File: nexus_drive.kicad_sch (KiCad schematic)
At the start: 0 parts

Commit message: Add phase power section to schematic from moteus x1
Three half-bridge sheets (FDMT80080DC pair, 0.5 mOhm shunt, Kelvin net
ties, gate clamp, phase pad) and the 36x 4.7uF DC-link bank, copied from
mjbots moteus hw/x1 (Apache-2.0) with attribution in NOTICE.md.

Co-Authored-By: Claude Opus 5.5 <noreply@anthropic.com>
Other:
- added sheet Bulk Capacitance (bulk_capacitance.kicad_sch)
- added sheet H Bridge A (h_bridge.kicad_sch)
- added sheet H Bridge B (h_bridge.kicad_sch)
- added sheet H Bridge C (h_bridge.kicad_sch)
- note added: "0.1 uF 100 V local decoupling, BAT41 low-side gate clamp, Kelvin net ties to SPx/SNx, M2.5 phase output pad."
- note added: "Bulk Capacitance = 36x 4.7 uF 100 V X7R DC-link bank between V+ and GNDPWR (global nets)."
- note added: "Copied from mjbots moteus-x1 r1 (Apache-2.0): https://github.com/mjbots/moteus/tree/main/hw/x1"
- note added: "Each H Bridge sheet = one half-bridge: 2x FDMT80080DC (80 V), 0.5 mOhm low-side shunt,"
- note added: "GHx/SHx/GLx/SPx/SNx connect to the DRV8353S gate driver sheet (to be added)."
- note added: "PHASE POWER STAGE"
- note added: "Still to add (see docs/power-stage.md): input TVS, bulk electrolytic, anti-spark connector, voltage dividers."
- title: (none) -> Nexus Drive

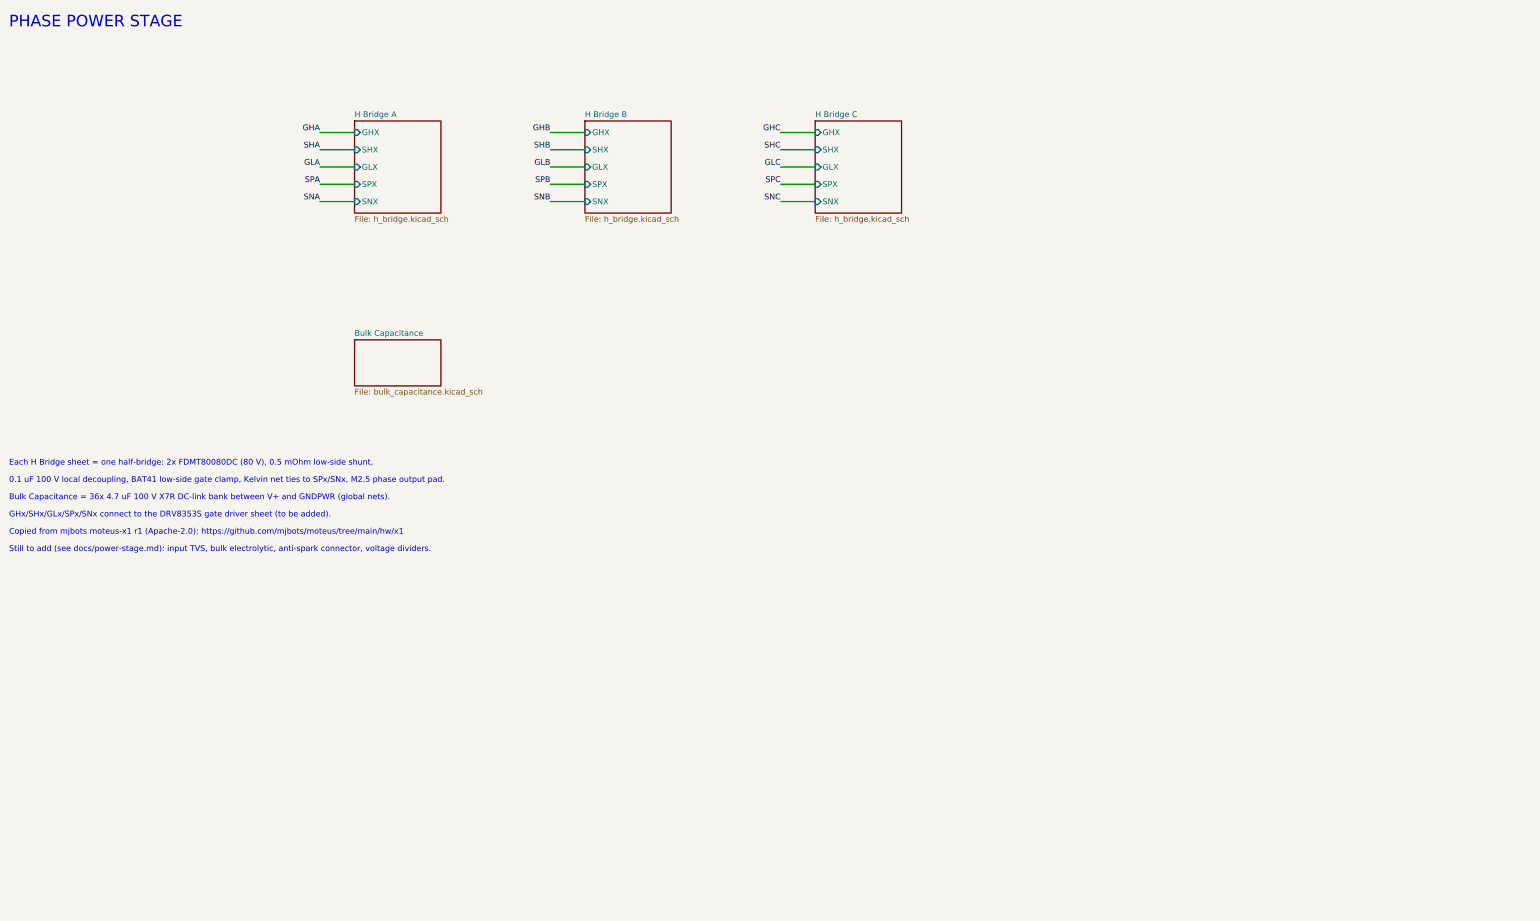
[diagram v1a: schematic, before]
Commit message: Add DRV8353S gate driver and current-sense filter sheets from moteus x1
Gate driver and current-sense RC sheets copied from mjbots moteus hw/x1
(Apache-2.0). Root sheet moved to A3 and rewired; netlist matches moteus
pin-for-pin for the driver and power stage.

Co-Authored-By: Claude Opus 5.5 <noreply@anthropic.com>
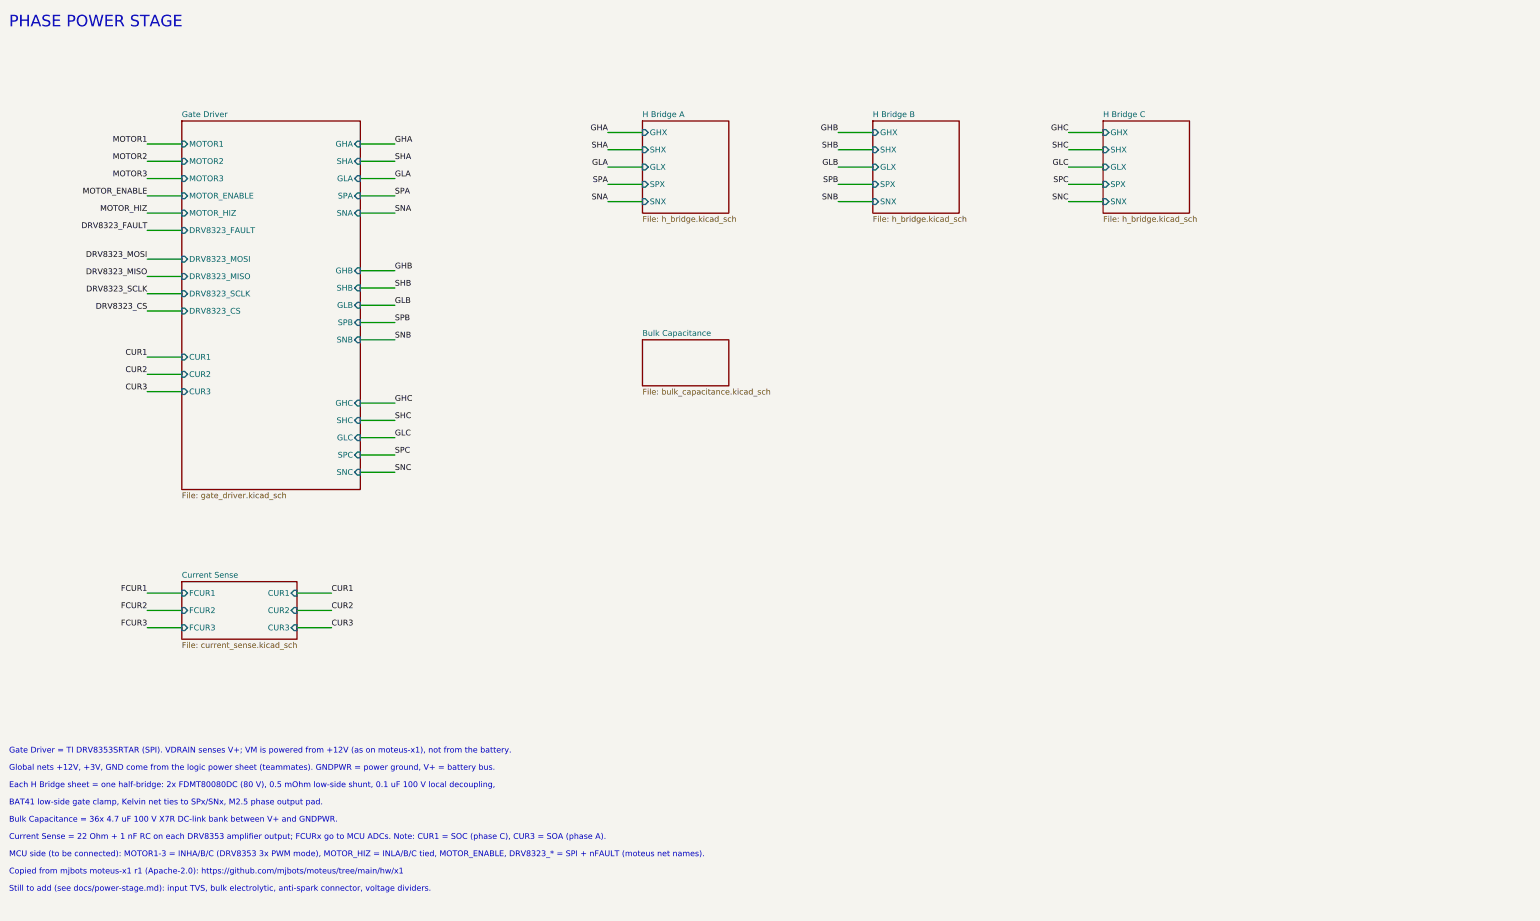
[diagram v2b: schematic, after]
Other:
- added sheet Current Sense (current_sense.kicad_sch)
- added sheet Gate Driver (gate_driver.kicad_sch)
- note added: "BAT41 low-side gate clamp, Kelvin net ties to SPx/SNx, M2.5 phase output pad."
- note added: "Bulk Capacitance = 36x 4.7 uF 100 V X7R DC-link bank between V+ and GNDPWR."
- note added: "Current Sense = 22 Ohm + 1 nF RC on each DRV8353 amplifier output; FCURx go to MCU ADCs. Note: CUR1 = SOC (phase C), CUR3 = SOA (phase A)."
- note added: "Each H Bridge sheet = one half-bridge: 2x FDMT80080DC (80 V), 0.5 mOhm low-side shunt, 0.1 uF 100 V local decoupling,"
- note added: "Gate Driver = TI DRV8353SRTAR (SPI). VDRAIN senses V+; VM is powered from +12V (as on moteus-x1), not from the battery."
- note added: "Global nets +12V, +3V, GND come from the logic power sheet (teammates). GNDPWR = power ground, V+ = battery bus."
- note added: "MCU side (to be connected): MOTOR1-3 = INHA/B/C (DRV8353 3x PWM mode), MOTOR_HIZ = INLA/B/C tied, MOTOR_ENABLE, DRV8323_* = SPI + nFAULT (moteus net names)."
- note removed: "0.1 uF 100 V local decoupling, BAT41 low-side gate clamp, Kelvin net ties to SPx/SNx, M2.5 phase output pad."
- note removed: "Bulk Capacitance = 36x 4.7 uF 100 V X7R DC-link bank between V+ and GNDPWR (global nets)."
- note removed: "Each H Bridge sheet = one half-bridge: 2x FDMT80080DC (80 V), 0.5 mOhm low-side shunt,"
- note removed: "GHx/SHx/GLx/SPx/SNx connect to the DRV8353S gate driver sheet (to be added)."

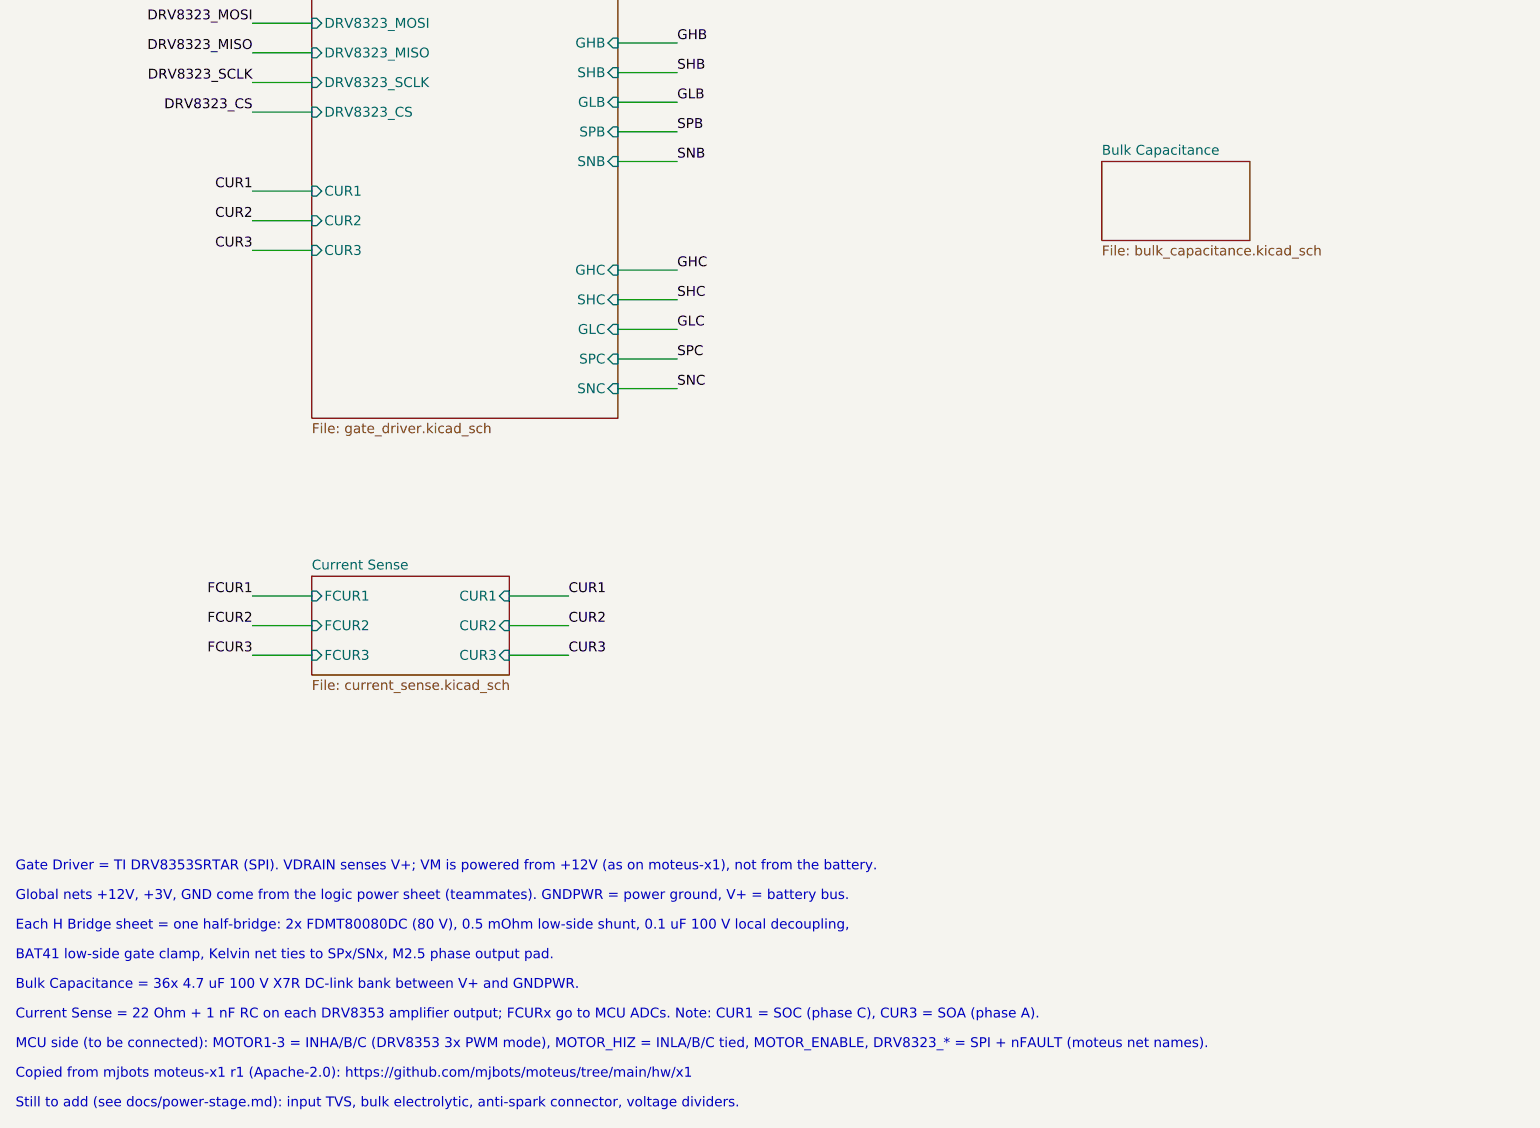
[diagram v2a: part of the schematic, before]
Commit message: Remove DC-link capacitor bank; note bulk capacitance in README
The ceramic DC-link bank is owned by another team member, so the Bulk
Capacitance sheet is removed. README explains why bulk capacitance
(electrolytic preferred over tantalum) is still needed.

Co-Authored-By: Claude Opus 5.5 <noreply@anthropic.com>
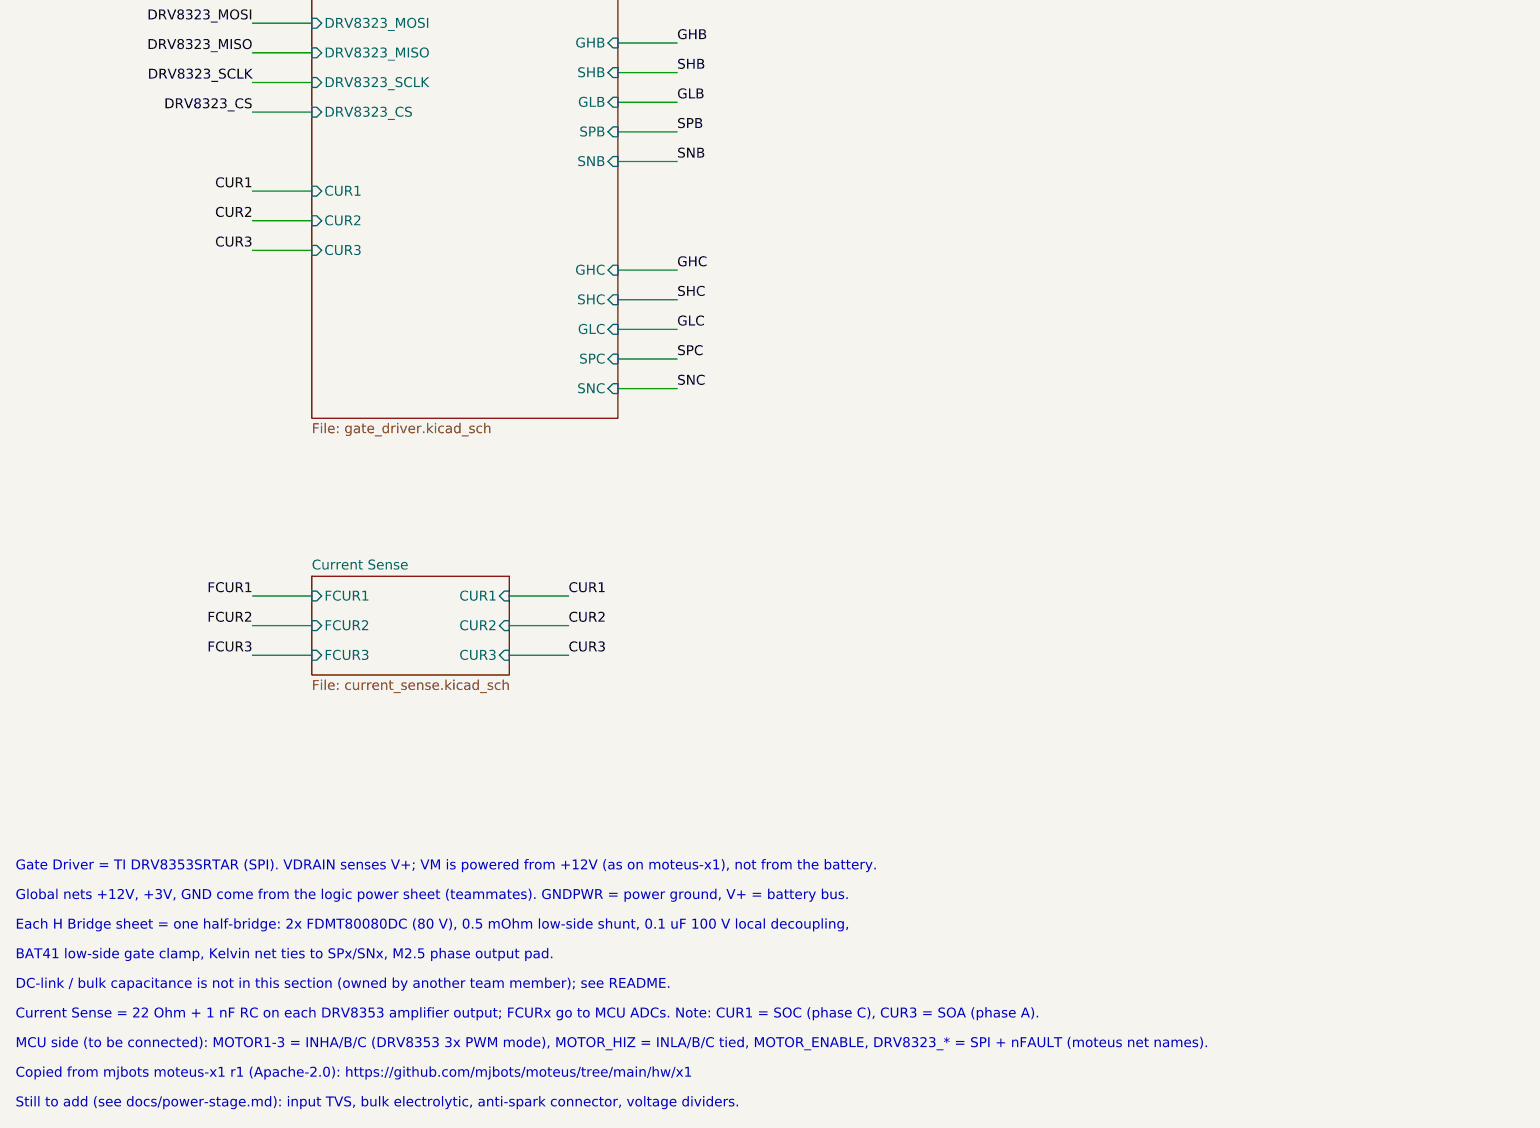
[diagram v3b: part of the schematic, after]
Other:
- removed sheet Bulk Capacitance
- note added: "DC-link / bulk capacitance is not in this section (owned by another team member); see README."
- note removed: "Bulk Capacitance = 36x 4.7 uF 100 V X7R DC-link bank between V+ and GNDPWR."
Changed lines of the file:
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@@
 			)
-	)
-	(sheet
-		(at 165.1 99.06)
-		(size 19.05 10.16)
-		(exclude_from_sim no)
-		(in_bom yes)
-		(on_board yes)
-		(dnp no)
-		(fields_autoplaced yes)
-		(stroke
-			(width 0.1524)
-			(type solid)
-		)
-		(fill
-			(color 0 0 0 0.0000)
-		)
-		(property "Sheetname" "Bulk Capacitance"
-			(at 165.1 98.3484 0)
-			(effects
-				(font
-					(size 1.27 1.27)
-				)
-				(justify left bottom)
-			)
-		)
-		(property "Sheetfile" "bulk_capacitance.kicad_sch"
-			(at 165.1 109.8046 0)
-			(effects
-				(font
-					(size 1.27 1.27)
-				)
-				(justify left top)
-			)
-		)
-		(instances
-			(project "nexus_drive"
-				(path "/2d97709d-a8ce-4889-9b37-2fa808653238"
-					(page "7")
-				)
-			)
-		)
 	)
 	(text "PHASE POWER STAGE"
@@
 		)
 	)
-	(text "Bulk Capacitance = 36x 4.7 uF 100 V X7R DC-link bank between V+ and GNDPWR."
+	(text "DC-link / bulk capacitance is not in this section (owned by another team member); see README."
 		(exclude_from_sim no)
 		(at 25.4 205.74 0)
